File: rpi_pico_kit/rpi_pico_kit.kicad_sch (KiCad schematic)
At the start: 2 parts, among them SW1 SW_Push_Dual, U1 Pico

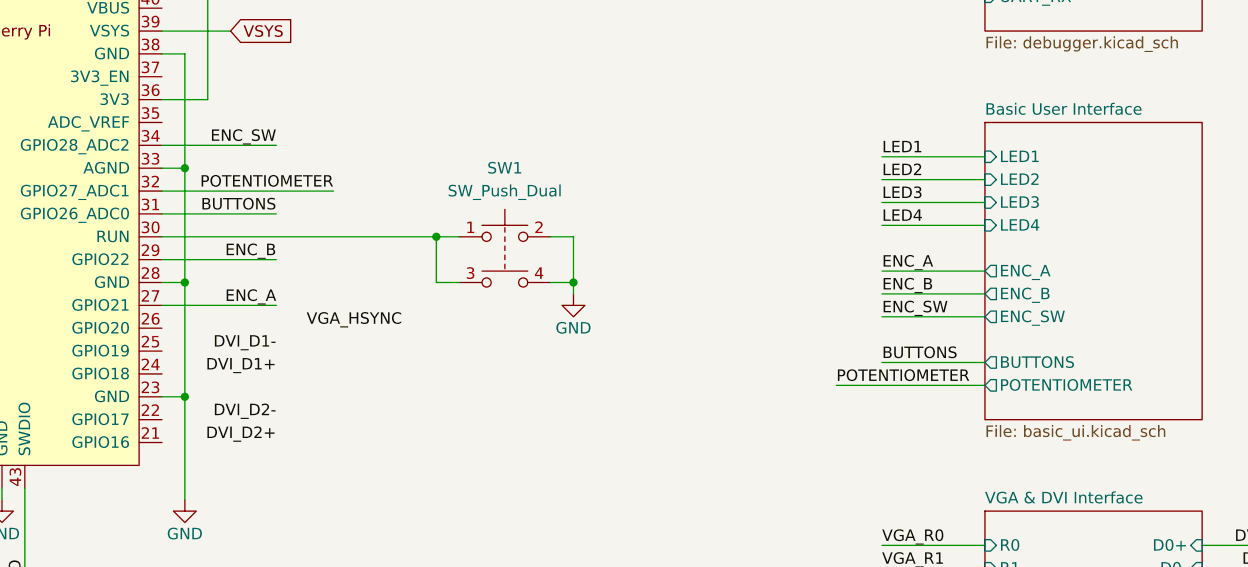
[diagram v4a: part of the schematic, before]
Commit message: removed dac buttons
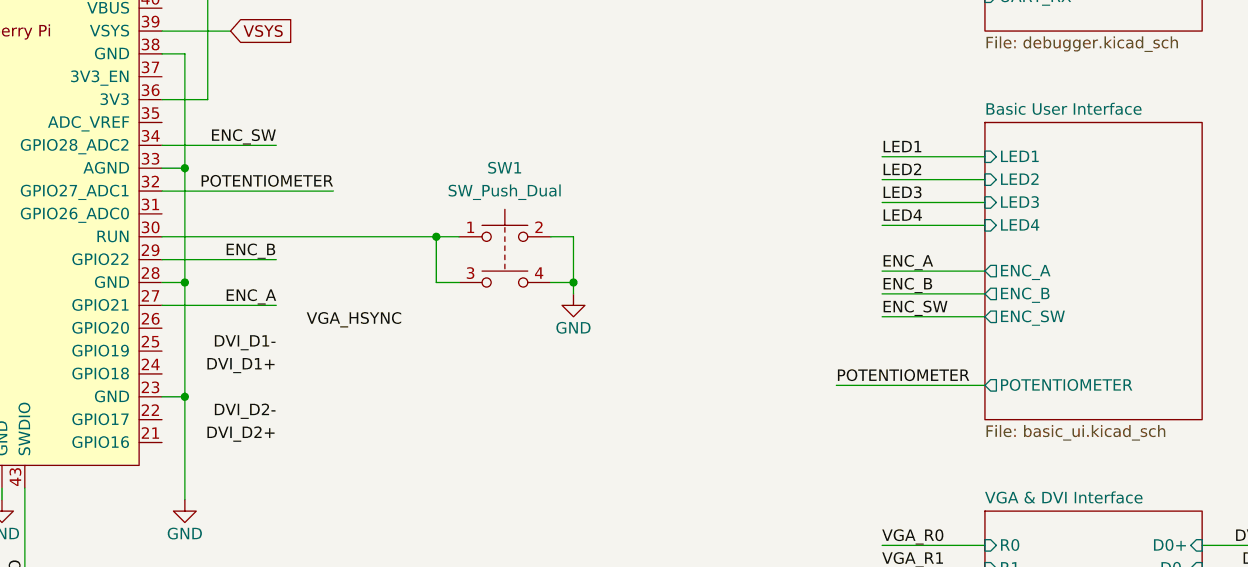
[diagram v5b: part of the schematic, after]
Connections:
- net BUTTONS: no longer names the net of U1.31 (GPIO26_ADC0)
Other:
- sheet Basic User Interface ports: added none; removed BUTTONS
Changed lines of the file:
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@@
-    (stroke (width 0) (type default) (color 0 0 0 0))
-  )
-  (wire (pts (xy 184.15 96.52) (xy 195.58 96.52))
     (stroke (width 0) (type default) (color 0 0 0 0))
   )
@@
     (stroke (width 0) (type default) (color 0 0 0 0))
   )
-  (wire (pts (xy 104.14 80.01) (xy 116.84 80.01))
-    (stroke (width 0) (type default) (color 0 0 0 0))
-  )
   (wire (pts (xy 66.04 62.23) (xy 66.04 74.93))
     (stroke (width 0) (type default) (color 0 0 0 0))
@@
     (effects (font (size 1.27 1.27)) (justify left bottom))
   )
-  (label "BUTTONS" (at 184.15 96.52 0)
-    (effects (font (size 1.27 1.27)) (justify left bottom))
-  )
   (label "VGA_HSYNC" (at 130.81 92.71 180)
     (effects (font (size 1.27 1.27)) (justify right bottom))
@@
   )
   (label "ENC_B" (at 116.84 85.09 180)
-    (effects (font (size 1.27 1.27)) (justify right bottom))
-  )
-  (label "BUTTONS" (at 116.84 80.01 180)
     (effects (font (size 1.27 1.27)) (justify right bottom))
   )
@@
       (effects (font (size 1.27 1.27)) (justify left))
     )
-    (pin "BUTTONS" output (at 195.58 96.52 180)
-      (effects (font (size 1.27 1.27)) (justify left))
-    )
   )
   (sheet (at 195.58 113.03) (size 24.13 34.29) (fields_autoplaced)
@@
     (path "/81612aa8-1e7d-439d-a45b-52594d29b291" (page "3"))
     (path "/9fa08ac3-227f-4cf0-bd88-360446d7d584" (page "4"))
-    (path "/81612aa8-1e7d-439d-a45b-52594d29b291/0065707f-10bf-4ce6-8c87-b586b6aef774" (page "5"))
   )
   (symbol_instances
@@
       (reference "#PWR046") (unit 1) (value "GND") (footprint "")
     )
-    (path "/81612aa8-1e7d-439d-a45b-52594d29b291/0065707f-10bf-4ce6-8c87-b586b6aef774/08d14a2d-378c-4de0-b866-288e2a817786"
-      (reference "#PWR?") (unit 1) (value "GND") (footprint "")
-    )
-    (path "/81612aa8-1e7d-439d-a45b-52594d29b291/0065707f-10bf-4ce6-8c87-b586b6aef774/09909c0f-acf4-441d-a2fe-f27e31895e91"
-      (reference "#PWR?") (unit 1) (value "GND") (footprint "")
-    )
-    (path "/81612aa8-1e7d-439d-a45b-52594d29b291/0065707f-10bf-4ce6-8c87-b586b6aef774/1327e1ff-4af1-4681-b7f1-be4d71b6f6e1"
-      (reference "#PWR?") (unit 1) (value "GND") (footprint "")
-    )
-    (path "/81612aa8-1e7d-439d-a45b-52594d29b291/0065707f-10bf-4ce6-8c87-b586b6aef774/21ba91e0-1f08-4ab5-8b97-a4d79d04b2dd"
-      (reference "#PWR?") (unit 1) (value "GND") (footprint "")
-    )
-    (path "/81612aa8-1e7d-439d-a45b-52594d29b291/0065707f-10bf-4ce6-8c87-b586b6aef774/2d32291a-67af-4211-bd36-aea63ed4c6ce"
-      (reference "#PWR?") (unit 1) (value "GND") (footprint "")
-    )
-    (path "/81612aa8-1e7d-439d-a45b-52594d29b291/0065707f-10bf-4ce6-8c87-b586b6aef774/4b3e5db0-90e2-4ce1-808f-6746afaad629"
-      (reference "#PWR?") (unit 1) (value "GND") (footprint "")
-    )
-    (path "/81612aa8-1e7d-439d-a45b-52594d29b291/0065707f-10bf-4ce6-8c87-b586b6aef774/547f4a2a-eea0-4deb-9650-fa0d78919ced"
-      (reference "#PWR?") (unit 1) (value "GND") (footprint "")
-    )
-    (path "/81612aa8-1e7d-439d-a45b-52594d29b291/0065707f-10bf-4ce6-8c87-b586b6aef774/61a3aaa4-668e-433a-92f6-0307ee293dc8"
-      (reference "#PWR?") (unit 1) (value "GND") (footprint "")
-    )
-    (path "/81612aa8-1e7d-439d-a45b-52594d29b291/0065707f-10bf-4ce6-8c87-b586b6aef774/750e807e-2a5e-46bd-80ea-0a4908221d71"
-      (reference "#PWR?") (unit 1) (value "+3.3V") (footprint "")
-    )
-    (path "/81612aa8-1e7d-439d-a45b-52594d29b291/0065707f-10bf-4ce6-8c87-b586b6aef774/80ec06b5-8ccf-422c-a999-945a761e0c8d"
-      (reference "#PWR?") (unit 1) (value "GND") (footprint "")
-    )
-    (path "/81612aa8-1e7d-439d-a45b-52594d29b291/0065707f-10bf-4ce6-8c87-b586b6aef774/89ccafdf-3478-4b64-ae17-dffe858f437e"
-      (reference "#PWR?") (unit 1) (value "GND") (footprint "")
-    )
-    (path "/81612aa8-1e7d-439d-a45b-52594d29b291/0065707f-10bf-4ce6-8c87-b586b6aef774/c88b01b5-5ac6-4c57-ad26-63a71b733bd4"
-      (reference "#PWR?") (unit 1) (value "+3.3V") (footprint "")
-    )
     (path "/81612aa8-1e7d-439d-a45b-52594d29b291/8282c2fc-13c2-4ba9-8d93-6cfca971b980"
       (reference "C1") (unit 1) (value "10n") (footprint "")
@@
       (reference "R47") (unit 1) (value "270R") (footprint "Resistor_SMD:R_0805_2012Metric_Pad1.20x1.40mm_HandSolder")
     )
-    (path "/81612aa8-1e7d-439d-a45b-52594d29b291/0065707f-10bf-4ce6-8c87-b586b6aef774/055209d0-4c5f-40c1-bfd0-b9b7ef40c4fb"
-      (reference "R?") (unit 1) (value "1k") (footprint "Resistor_SMD:R_0805_2012Metric_Pad1.20x1.40mm_HandSolder")
-    )
-    (path "/81612aa8-1e7d-439d-a45b-52594d29b291/0065707f-10bf-4ce6-8c87-b586b6aef774/1f6c76ca-febf-4d2e-a4b0-4ff602b73940"
-      (reference "R?") (unit 1) (value "2k") (footprint "Resistor_SMD:R_0805_2012Metric_Pad1.20x1.40mm_HandSolder")
-    )
-    (path "/81612aa8-1e7d-439d-a45b-52594d29b291/0065707f-10bf-4ce6-8c87-b586b6aef774/44b92634-0f0e-4a49-96a1-fc293467756d"
-      (reference "R?") (unit 1) (value "1k") (footprint "Resistor_SMD:R_0805_2012Metric_Pad1.20x1.40mm_HandSolder")
-    )
-    (path "/81612aa8-1e7d-439d-a45b-52594d29b291/0065707f-10bf-4ce6-8c87-b586b6aef774/45d17eec-991a-41a3-950a-af34299a6bf7"
-      (reference "R?") (unit 1) (value "1k") (footprint "Resistor_SMD:R_0805_2012Metric_Pad1.20x1.40mm_HandSolder")
-    )
-    (path "/81612aa8-1e7d-439d-a45b-52594d29b291/0065707f-10bf-4ce6-8c87-b586b6aef774/7aadb5c7-7484-40a0-a0fb-aa07b41dbba5"
-      (reference "R?") (unit 1) (value "2k") (footprint "Resistor_SMD:R_0805_2012Metric_Pad1.20x1.40mm_HandSolder")
-    )
-    (path "/81612aa8-1e7d-439d-a45b-52594d29b291/0065707f-10bf-4ce6-8c87-b586b6aef774/8c680327-54d2-47dd-9767-9c0fb4ad158f"
-      (reference "R?") (unit 1) (value "2k") (footprint "Resistor_SMD:R_0805_2012Metric_Pad1.20x1.40mm_HandSolder")
-    )
-    (path "/81612aa8-1e7d-439d-a45b-52594d29b291/0065707f-10bf-4ce6-8c87-b586b6aef774/8e8c4c98-07cd-4210-bdbf-8559d22c34a8"
-      (reference "R?") (unit 1) (value "1k") (footprint "Resistor_SMD:R_0805_2012Metric_Pad1.20x1.40mm_HandSolder")
-    )
-    (path "/81612aa8-1e7d-439d-a45b-52594d29b291/0065707f-10bf-4ce6-8c87-b586b6aef774/a7b13de1-8782-490a-a548-c504733257ec"
-      (reference "R?") (unit 1) (value "1k") (footprint "Resistor_SMD:R_0805_2012Metric_Pad1.20x1.40mm_HandSolder")
-    )
-    (path "/81612aa8-1e7d-439d-a45b-52594d29b291/0065707f-10bf-4ce6-8c87-b586b6aef774/c94434cd-20f1-4bdd-b7f6-1b294db5e89b"
-      (reference "R?") (unit 1) (value "2k") (footprint "Resistor_SMD:R_0805_2012Metric_Pad1.20x1.40mm_HandSolder")
-    )
-    (path "/81612aa8-1e7d-439d-a45b-52594d29b291/0065707f-10bf-4ce6-8c87-b586b6aef774/c953be6d-96c5-4725-b8c4-2b69df97118b"
-      (reference "R?") (unit 1) (value "1k") (footprint "Resistor_SMD:R_0805_2012Metric_Pad1.20x1.40mm_HandSolder")
-    )
-    (path "/81612aa8-1e7d-439d-a45b-52594d29b291/0065707f-10bf-4ce6-8c87-b586b6aef774/d0d72cc0-1e86-4d93-adb3-0fbb6ce3b111"
-      (reference "R?") (unit 1) (value "2k") (footprint "Resistor_SMD:R_0805_2012Metric_Pad1.20x1.40mm_HandSolder")
-    )
-    (path "/81612aa8-1e7d-439d-a45b-52594d29b291/0065707f-10bf-4ce6-8c87-b586b6aef774/e09d3b7a-8a05-4b2b-9ffe-7f94e092ef90"
-      (reference "R?") (unit 1) (value "1k") (footprint "Resistor_SMD:R_0805_2012Metric_Pad1.20x1.40mm_HandSolder")
-    )
     (path "/81612aa8-1e7d-439d-a45b-52594d29b291/1911cdc8-cf7d-4aba-aec2-0c4898a95145"
       (reference "RV1") (unit 1) (value "10k") (footprint "Potentiometer_THT:Potentiometer_Alpha_RD901F-40-00D_Single_Vertical")
@@
       (reference "SW6") (unit 1) (value "RotaryEncoder_Switch") (footprint "")
     )
-    (path "/81612aa8-1e7d-439d-a45b-52594d29b291/0065707f-10bf-4ce6-8c87-b586b6aef774/328e09e5-7df7-4fea-ac05-269c471ea2ea"
-      (reference "SW?") (unit 1) (value "SW_Push_Dual") (footprint "")
-    )
-    (path "/81612aa8-1e7d-439d-a45b-52594d29b291/0065707f-10bf-4ce6-8c87-b586b6aef774/58751830-60d1-4c89-8468-75ad276677d0"
-      (reference "SW?") (unit 1) (value "SW_Push_Dual") (footprint "")
-    )
-    (path "/81612aa8-1e7d-439d-a45b-52594d29b291/0065707f-10bf-4ce6-8c87-b586b6aef774/877979a3-ec0a-4a3e-a42b-d26a2cb89869"
-      (reference "SW?") (unit 1) (value "SW_Push_Dual") (footprint "")
-    )
-    (path "/81612aa8-1e7d-439d-a45b-52594d29b291/0065707f-10bf-4ce6-8c87-b586b6aef774/ebb33032-edcf-48ab-b440-fe3ea4cdfdbe"
-      (reference "SW?") (unit 1) (value "SW_Push_Dual") (footprint "")
-    )
     (path "/8f624921-0bb1-4d0e-848b-7458a506535e"
       (reference "U1") (unit 1) (value "Pico") (footprint "RPi_Pico:RPi_Pico_SMD_TH")
@@
       (reference "U3") (unit 1) (value "RP2040") (footprint "RP2040_minimal:RP2040-QFN-56")
     )
-    (path "/81612aa8-1e7d-439d-a45b-52594d29b291/0065707f-10bf-4ce6-8c87-b586b6aef774/1ad15fb7-3ec5-49e0-a7f6-c09338c26493"
-      (reference "U?") (unit 1) (value "74LS125") (footprint "Package_DIP:DIP-14_W7.62mm_Socket_LongPads")
-    )
-    (path "/81612aa8-1e7d-439d-a45b-52594d29b291/0065707f-10bf-4ce6-8c87-b586b6aef774/cf9e257f-cabb-4531-abc9-4a8b0aecd0ba"
-      (reference "U?") (unit 2) (value "74LS125") (footprint "Package_DIP:DIP-14_W7.62mm_Socket_LongPads")
-    )
-    (path "/81612aa8-1e7d-439d-a45b-52594d29b291/0065707f-10bf-4ce6-8c87-b586b6aef774/26aa5fcc-3c5c-4379-bb25-c6e6e3c6d50a"
-      (reference "U?") (unit 3) (value "74LS125") (footprint "Package_DIP:DIP-14_W7.62mm_Socket_LongPads")
-    )
-    (path "/81612aa8-1e7d-439d-a45b-52594d29b291/0065707f-10bf-4ce6-8c87-b586b6aef774/dbf2ec6d-5b7c-4864-8414-3433d3b742de"
-      (reference "U?") (unit 4) (value "74LS125") (footprint "Package_DIP:DIP-14_W7.62mm_Socket_LongPads")
-    )
-    (path "/81612aa8-1e7d-439d-a45b-52594d29b291/0065707f-10bf-4ce6-8c87-b586b6aef774/517a450e-278d-475d-a9e2-411a3700258d"
-      (reference "U?") (unit 5) (value "74LS125") (footprint "Package_DIP:DIP-14_W7.62mm_Socket_LongPads")
-    )
-  )
+  )

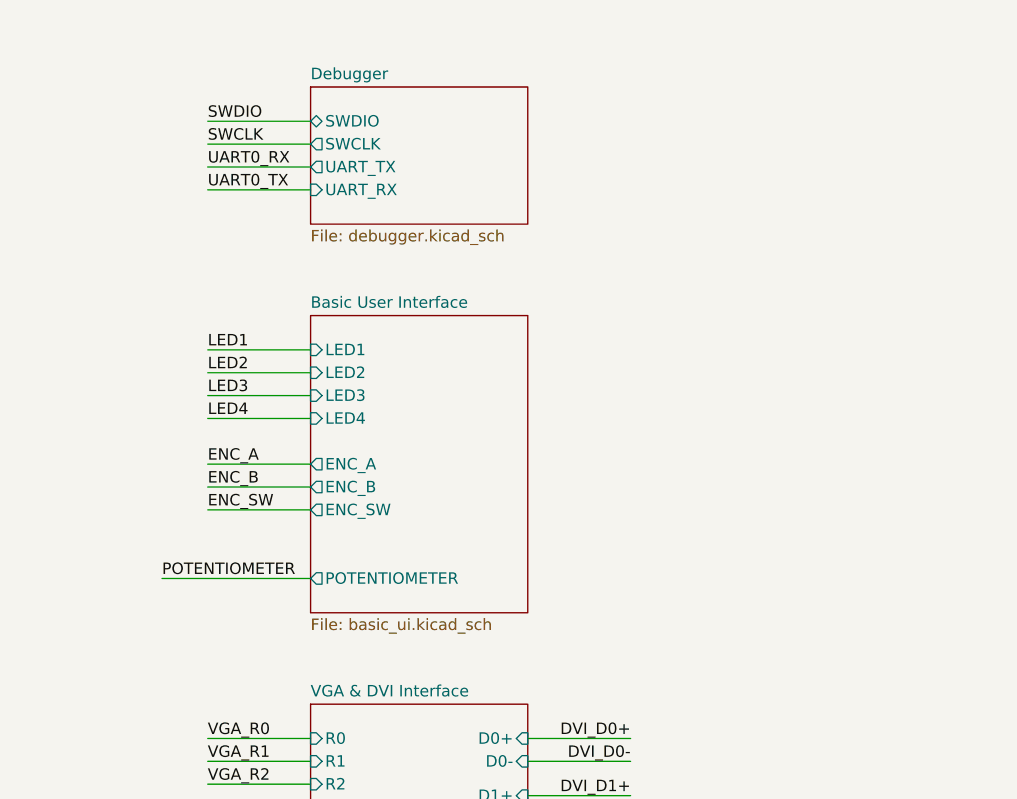
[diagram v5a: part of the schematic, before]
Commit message: added SPI devices
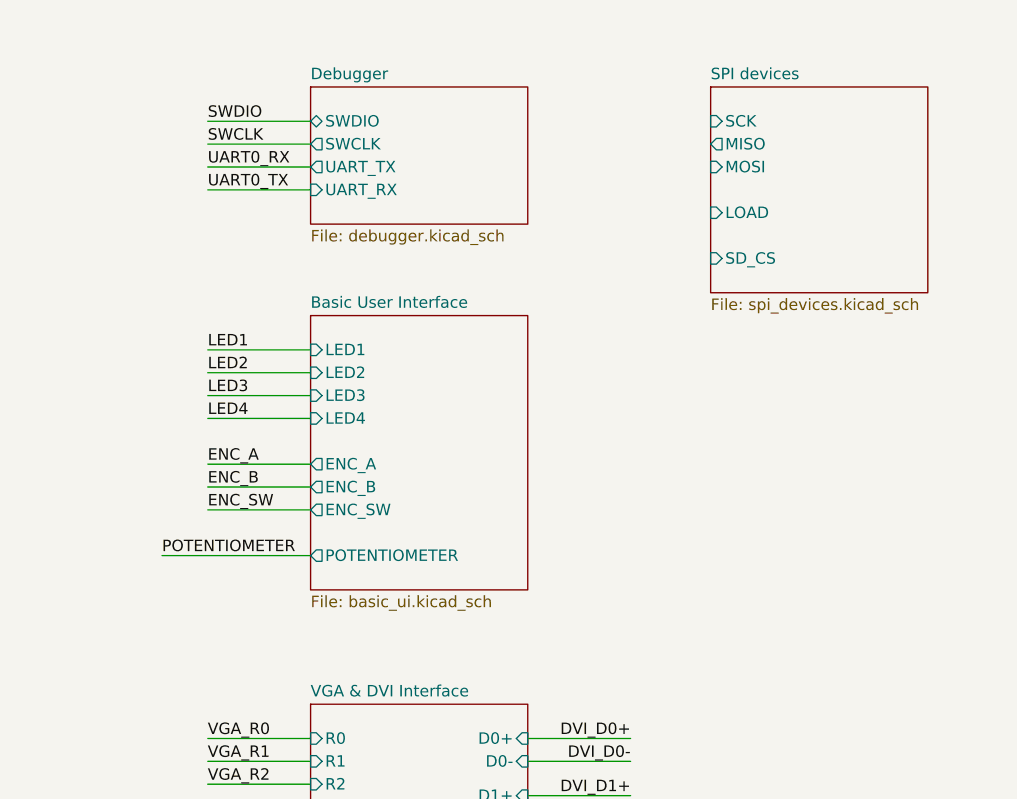
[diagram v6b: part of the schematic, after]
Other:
- added sheet SPI devices (spi_devices.kicad_sch)

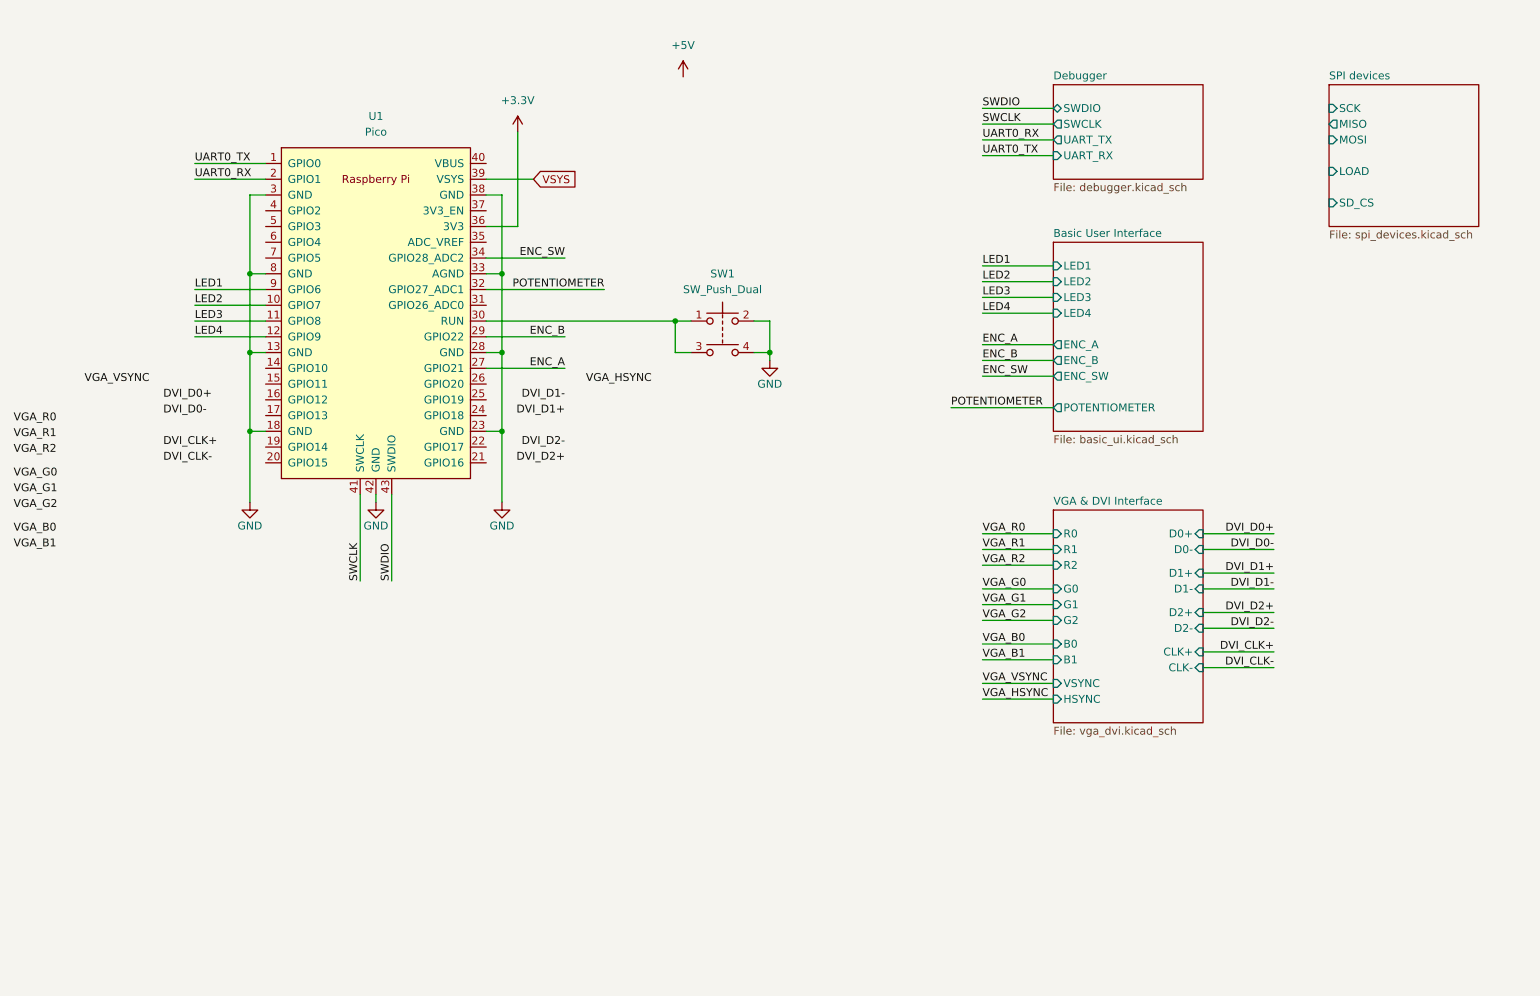
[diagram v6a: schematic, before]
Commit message: added i2c and audio interface
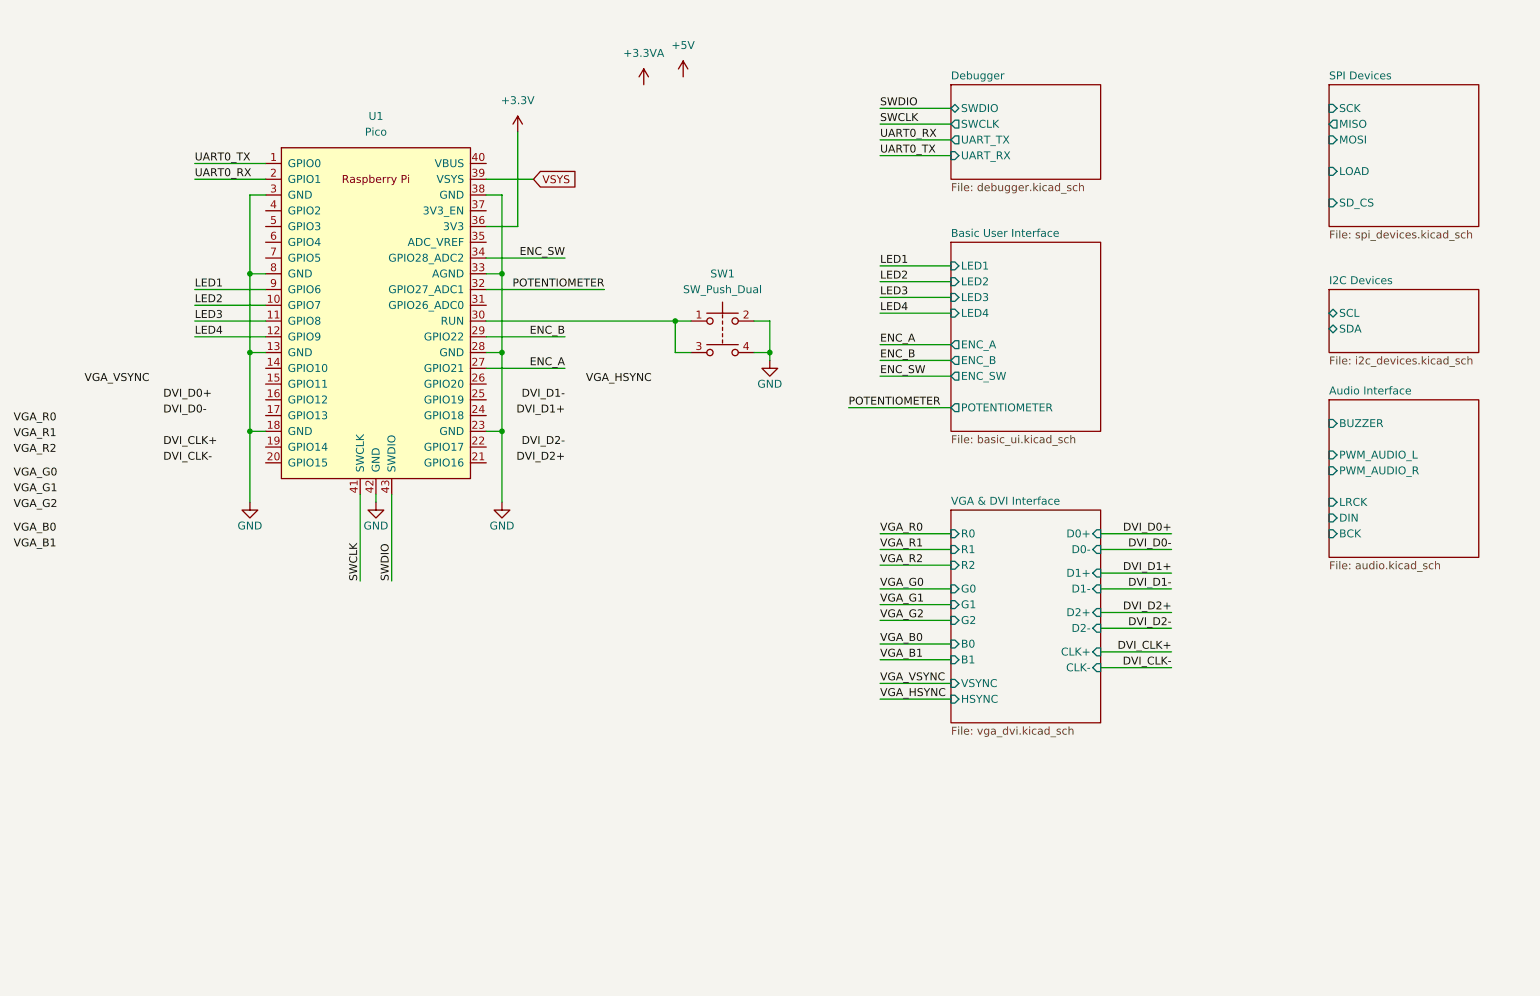
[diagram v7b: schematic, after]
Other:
- sheet SPI devices renamed SPI Devices
- added sheet Audio Interface (audio.kicad_sch)
- added sheet I2C Devices (i2c_devices.kicad_sch)
